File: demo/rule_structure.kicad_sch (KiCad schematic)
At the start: 0 parts

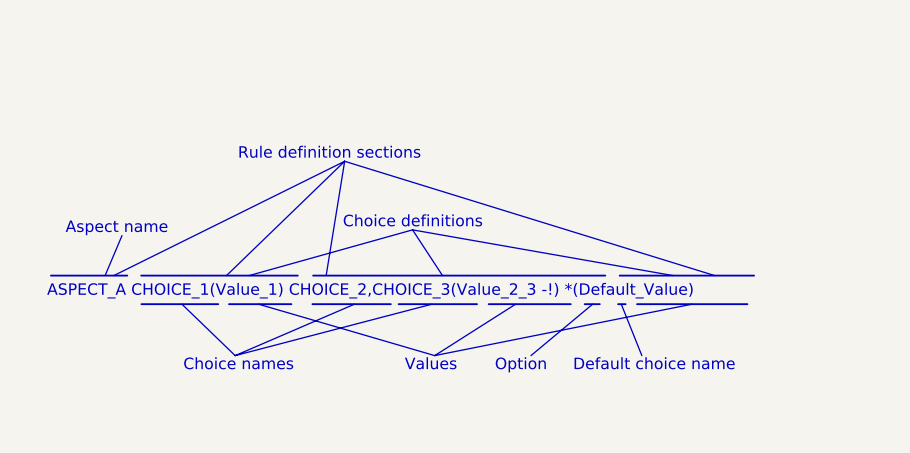
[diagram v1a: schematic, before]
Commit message: Make use of new 0.2.0 features in demo project, use different expression types
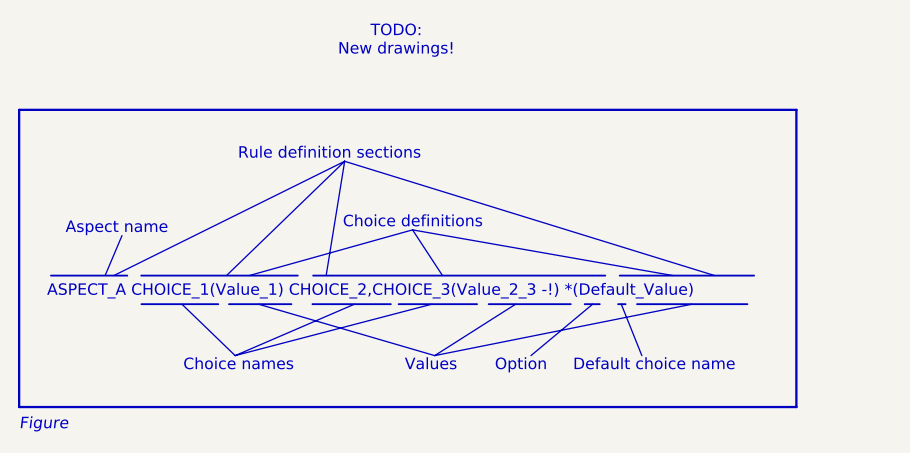
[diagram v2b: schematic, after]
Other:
- note added: "Figure"
- note added: "TODO: New drawings!"
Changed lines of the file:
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@@
+		)
+	)
+	(rectangle
+		(start 62.23 45.72)
+		(end 148.59 78.74)
+		(stroke
+			(width 0.254)
+			(type default)
+			(color 72 72 72 1)
+		)
+		(fill
+			(type none)
+		)
+	)
+	(text "TODO:\nNew drawings!"
+		(exclude_from_sim no)
+		(at 104.14 38.1 0)
+		(effects
+			(font
+				(size 1.27 1.27)
+			)
+		)
+	)
+	(text "Figure"
+		(exclude_from_sim no)
+		(at 62.23 80.01 0)
+		(effects
+			(font
+				(size 1.27 1.27)
+				(italic yes)
+				(color 72 72 72 1)
+			)
+			(justify left top)
 		)
 	)
